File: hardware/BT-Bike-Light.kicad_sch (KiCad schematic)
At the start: 15 parts, among them J1 Conn_ARM_JTAG_SWD_10, J2 USB_C_Receptacle_USB2.0_16P, J3 Conn_01x02, Q1 Q_NMOS_GDS, SW1 SW_Push, U1 BC805M, U2 LIS2DTW12, U3 PAM2808, U4 BQ297xy, U5 MCP73834-xxx-MF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

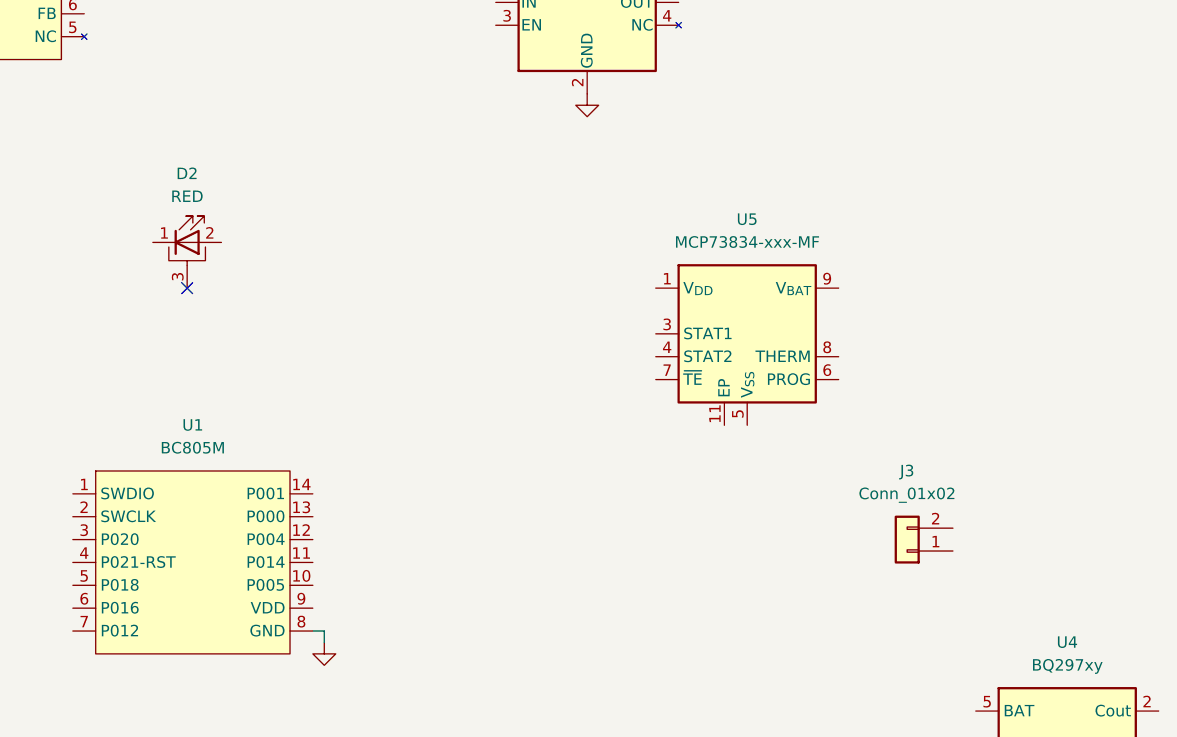
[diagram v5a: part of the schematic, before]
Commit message: Update battery connector
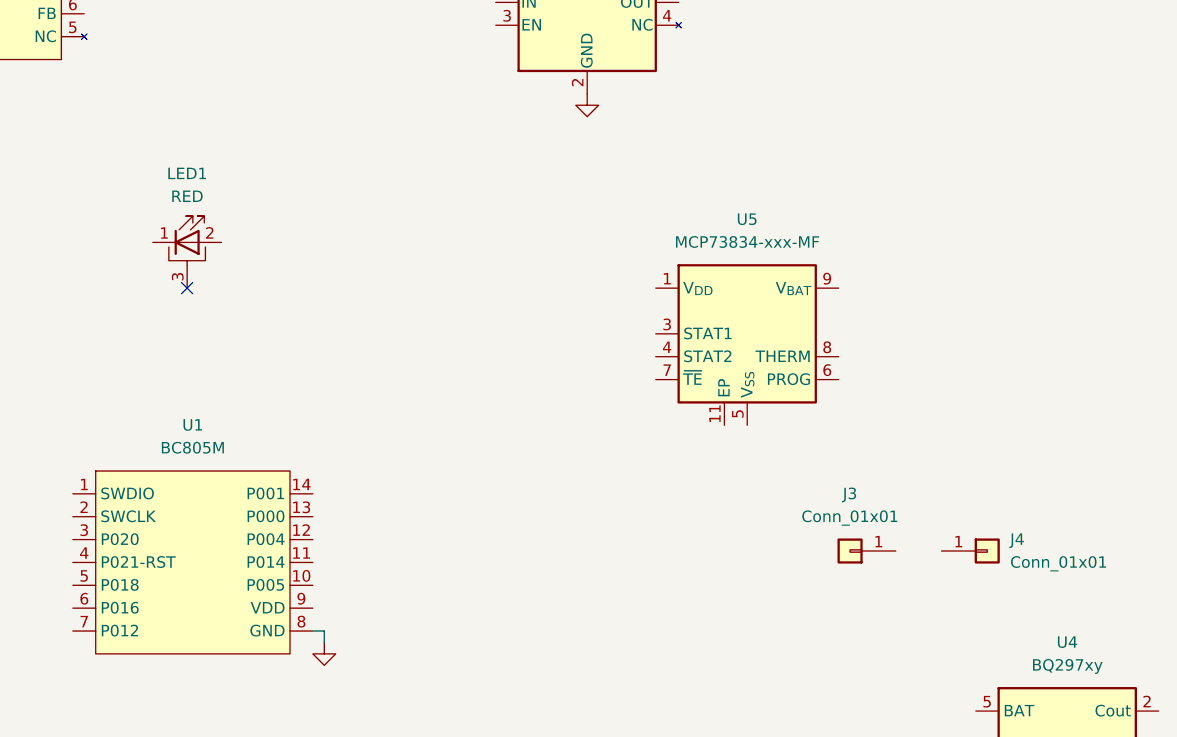
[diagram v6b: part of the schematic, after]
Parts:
- removed J3: Conn_01x02, symbol Connector_Generic:Conn_01x02
- added J3, J4: Conn_01x01, Battery:BatteryClip_Keystone_54_D16-19mm, symbol Connector_Generic:Conn_01x01
- renumbered D2 to LED1
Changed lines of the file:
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@@
+	)
+	(symbol
+		(lib_id "Connector_Generic:Conn_01x01")
+		(at 228.6 99.06 0)
+		(unit 1)
+		(exclude_from_sim no)
+		(in_bom yes)
+		(on_board yes)
+		(dnp no)
+		(fields_autoplaced yes)
+		(property "Reference" "J4"
+			(at 231.14 97.7899 0)
+			(effects
+				(font
+					(size 1.27 1.27)
+				)
+				(justify left)
+			)
+		)
+		(property "Value" "Conn_01x01"
+			(at 231.14 100.3299 0)
+			(effects
+				(font
+					(size 1.27 1.27)
+				)
+				(justify left)
+			)
+		)
+		(property "Footprint" "Battery:BatteryClip_Keystone_54_D16-19mm"
+			(at 228.6 99.06 0)
+			(effects
+				(font
+					(size 1.27 1.27)
+				)
+				(hide yes)
+			)
+		)
+		(property "Datasheet" "https://www.keyelco.com/userAssets/file/M65p11.pdf"
+			(at 228.6 99.06 0)
+			(effects
+				(font
+					(size 1.27 1.27)
+				)
+				(hide yes)
+			)
+		)
+		(property "Description" "Generic connector, single row, 01x01, script generated (kicad-library-utils/schlib/autogen/connector/)"
+			(at 228.6 99.06 0)
+			(effects
+				(font
+					(size 1.27 1.27)
+				)
+				(hide yes)
+			)
+		)
+		(pin "1"
+		)
+		(instances
+			(project ""
+				(path "/3263b444-391f-435a-aeab-6f7fca8830e2"
+					(reference "J4")
+					(unit 1)
+				)
+			)
+		)
+	)
+	(symbol
+		(lib_id "Connector_Generic:Conn_01x01")
+		(at 213.36 99.06 180)
+		(unit 1)
+		(exclude_from_sim no)
+		(in_bom yes)
+		(on_board yes)
+		(dnp no)
+		(fields_autoplaced yes)
+		(property "Reference" "J3"
+			(at 213.36 92.71 0)
+			(effects
+				(font
+					(size 1.27 1.27)
+				)
+			)
+		)
+		(property "Value" "Conn_01x01"
+			(at 213.36 95.25 0)
+			(effects
+				(font
+					(size 1.27 1.27)
+				)
+			)
+		)
+		(property "Footprint" "Battery:BatteryClip_Keystone_54_D16-19mm"
+			(at 213.36 99.06 0)
+			(effects
+				(font
+					(size 1.27 1.27)
+				)
+				(hide yes)
+			)
+		)
+		(property "Datasheet" "https://www.keyelco.com/userAssets/file/M65p11.pdf"
+			(at 213.36 99.06 0)
+			(effects
+				(font
+					(size 1.27 1.27)
+				)
+				(hide yes)
+			)
+		)
+		(property "Description" "Generic connector, single row, 01x01, script generated (kicad-library-utils/schlib/autogen/connector/)"
+			(at 213.36 99.06 0)
+			(effects
+				(font
+					(size 1.27 1.27)
+				)
+				(hide yes)
+			)
+		)
+		(pin "1"
+		)
+		(instances
+			(project "BT-Bike-Light"
+				(path "/3263b444-391f-435a-aeab-6f7fca8830e2"
+					(reference "J3")
+					(unit 1)
+				)
+			)
+		)
 	)
 	(symbol
@@
 		(dnp no)
 		(fields_autoplaced yes)
-		(property "Reference" "D2"
+		(property "Reference" "LED1"
 			(at 139.7 57.15 0)
 			(effects
@@
 			(project ""
 				(path "/3263b444-391f-435a-aeab-6f7fca8830e2"
-					(reference "D2")
+					(reference "LED1")
 					(unit 1)
 				)
@@
 					(unit 1)
 				)
-			)
-		)
-	)
-	(symbol
-		(lib_id "Connector_Generic:Conn_01x02")
-		(at 219.71 99.06 180)
-		(unit 1)
-		(exclude_from_sim no)
-		(in_bom yes)
-		(on_board yes)
-		(dnp no)
-		(fields_autoplaced yes)
-		(property "Reference" "J3"
-			(at 219.71 90.17 0)
-			(effects
-				(font
-					(size 1.27 1.27)
-				)
-			)
-		)
-		(property "Value" "Conn_01x02"
-			(at 219.71 92.71 0)
-			(effects
-				(font
-					(size 1.27 1.27)
-				)
-			)
-		)
-		(property "Footprint" ""
-			(at 219.71 99.06 0)
-			(effects
-				(font
-					(size 1.27 1.27)
-				)
-				(hide yes)
-			)
-		)
-		(property "Datasheet" "~"
-			(at 219.71 99.06 0)
-			(effects
-				(font
-					(size 1.27 1.27)
-				)
-				(hide yes)
-			)
-		)
-		(property "Description" "Generic connector, single row, 01x02, script generated (kicad-library-utils/schlib/autogen/connector/)"
-			(at 219.71 99.06 0)
-			(effects
-				(font
-					(size 1.27 1.27)
-				)
-				(hide yes)
-			)
-		)
-		(pin "2"
-		)
-		(pin "1"
-		)
-		(instances
-			(project ""
-				(path "/3263b444-391f-435a-aeab-6f7fca8830e2"
-					(reference "J3")
-					(unit 1)
-				)

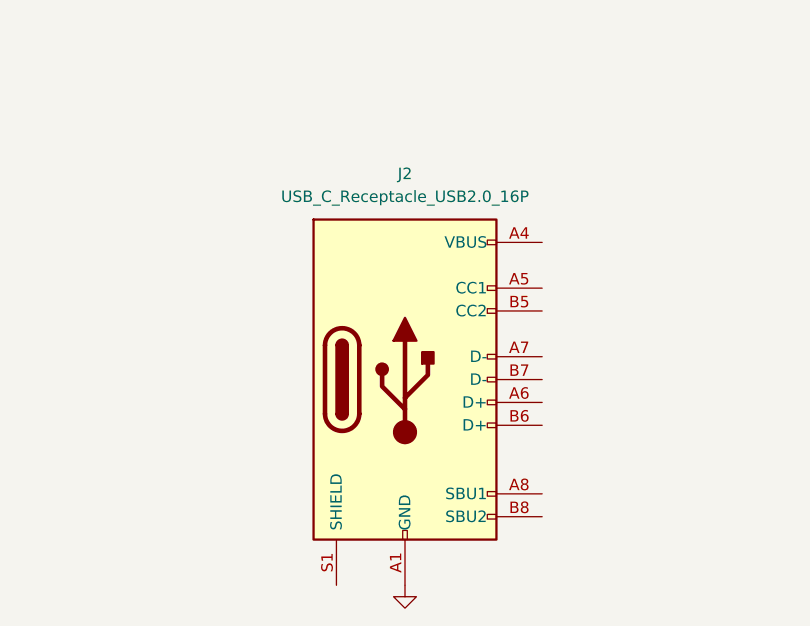
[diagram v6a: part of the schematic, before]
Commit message: Update USB-C receptacle
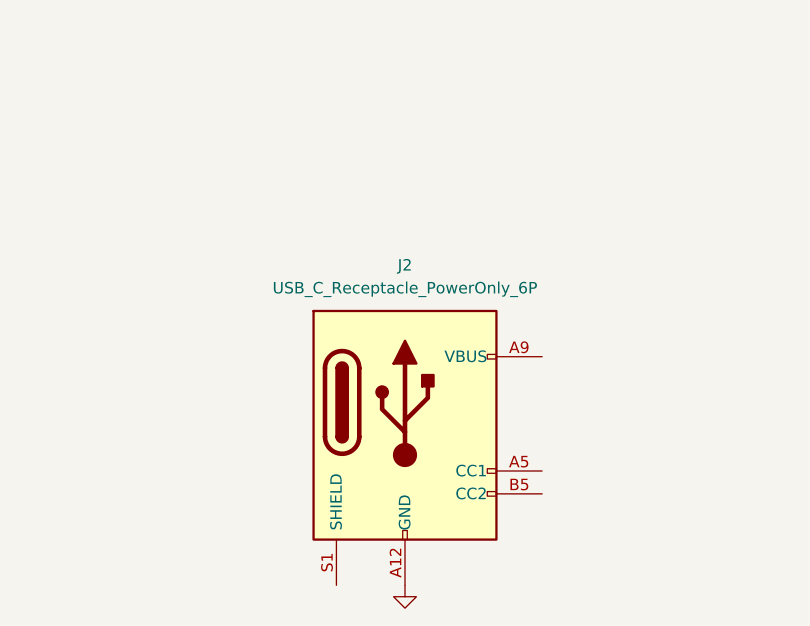
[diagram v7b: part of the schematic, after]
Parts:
- removed J2: USB_C_Receptacle_USB2.0_16P, GCT:USB_C_Receptacle_GCT_USB4145, symbol Connector:USB_C_Receptacle_USB2.0_16P
- added J2: USB_C_Receptacle_PowerOnly_6P, CUI-Devices:UJC-HP2-3-SMT-TR, symbol Connector:USB_C_Receptacle_PowerOnly_6P
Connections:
- net GND: now also J2.A12 (GND), J2.B12 (GND)
- new net: J2.A9 (VBUS), J2.B9 (VBUS)
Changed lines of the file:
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@@
-	)
-	(symbol
-		(lib_id "Connector:USB_C_Receptacle_USB2.0_16P")
-		(at 87.63 160.02 0)
-		(unit 1)
-		(exclude_from_sim no)
-		(in_bom yes)
-		(on_board yes)
-		(dnp no)
-		(fields_autoplaced yes)
-		(property "Reference" "J2"
-			(at 87.63 137.16 0)
-			(effects
-				(font
-					(size 1.27 1.27)
-				)
-			)
-		)
-		(property "Value" "USB_C_Receptacle_USB2.0_16P"
-			(at 87.63 139.7 0)
-			(effects
-				(font
-					(size 1.27 1.27)
-				)
-			)
-		)
-		(property "Footprint" "GCT:USB_C_Receptacle_GCT_USB4145"
-			(at 91.44 160.02 0)
-			(effects
-				(font
-					(size 1.27 1.27)
-				)
-				(hide yes)
-			)
-		)
-		(property "Datasheet" "https://www.usb.org/sites/default/files/documents/usb_type-c.zip"
-			(at 91.44 160.02 0)
-			(effects
-				(font
-					(size 1.27 1.27)
-				)
-				(hide yes)
-			)
-		)
-		(property "Description" "USB 2.0-only 16P Type-C Receptacle connector"
-			(at 87.63 160.02 0)
-			(effects
-				(font
-					(size 1.27 1.27)
-				)
-				(hide yes)
-			)
-		)
-		(pin "A12"
-		)
-		(pin "A6"
-		)
-		(pin "A8"
-		)
-		(pin "S1"
-		)
-		(pin "A4"
-		)
-		(pin "A7"
-		)
-		(pin "A5"
-		)
-		(pin "B8"
-		)
-		(pin "B7"
-		)
-		(pin "B9"
-		)
-		(pin "B1"
-		)
-		(pin "A1"
-		)
-		(pin "B6"
-		)
-		(pin "B5"
-		)
-		(pin "A9"
-		)
-		(pin "B4"
-		)
-		(pin "B12"
-		)
-		(instances
-			(project ""
-				(path "/3263b444-391f-435a-aeab-6f7fca8830e2"
-					(reference "J2")
-					(unit 1)
-				)
-			)
-		)
 	)
 	(symbol
@@
 					(unit 1)
 				)
+			)
+		)
+	)
+	(symbol
+		(lib_id "Connector:USB_C_Receptacle_PowerOnly_6P")
+		(at 87.63 165.1 0)
+		(unit 1)
+		(exclude_from_sim no)
+		(in_bom yes)
+		(on_board yes)
+		(dnp no)
+		(fields_autoplaced yes)
+		(property "Reference" "J2"
+			(at 87.63 147.32 0)
+			(effects
+				(font
+					(size 1.27 1.27)
+				)
+			)
+		)
+		(property "Value" "USB_C_Receptacle_PowerOnly_6P"
+			(at 87.63 149.86 0)
+			(effects
+				(font
+					(size 1.27 1.27)
+				)
+			)
+		)
+		(property "Footprint" "CUI-Devices:UJC-HP2-3-SMT-TR"
+			(at 91.44 162.56 0)
+			(effects
+				(font
+					(size 1.27 1.27)
+				)
+				(hide yes)
+			)
+		)
+		(property "Datasheet" "https://www.usb.org/sites/default/files/documents/usb_type-c.zip"
+			(at 87.63 165.1 0)
+			(effects
+				(font
+					(size 1.27 1.27)
+				)
+				(hide yes)
+			)
+		)
+		(property "Description" "USB Power-Only 6P Type-C Receptacle connector"
+			(at 87.63 165.1 0)
+			(effects
+				(font
+					(size 1.27 1.27)
+				)
+				(hide yes)
+			)
+		)
+		(pin "B5"
+		)
+		(pin "A5"
+		)
+		(pin "A12"
+		)
+		(pin "B12"
+		)
+		(pin "A9"
+		)
+		(pin "S1"
+		)
+		(pin "B9"
+		)
+		(instances
+			(project ""
+				(path "/3263b444-391f-435a-aeab-6f7fca8830e2"
+					(reference "J2")
+					(unit 1)
+				)

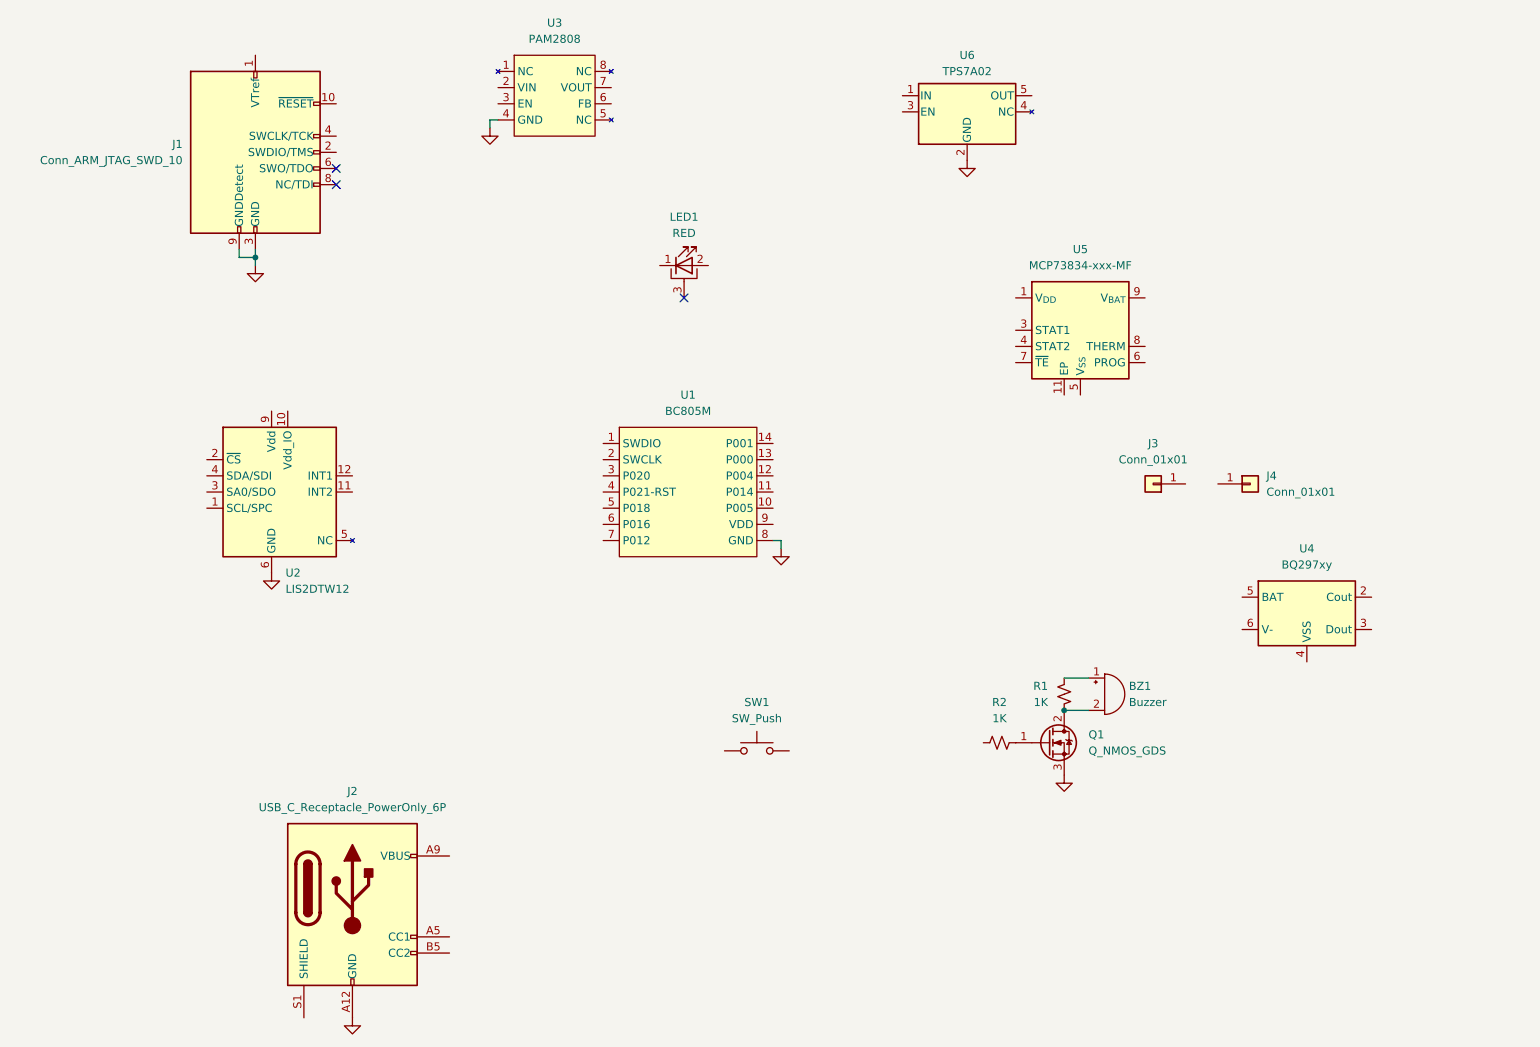
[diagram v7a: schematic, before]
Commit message: Add supporting electronics for LDO
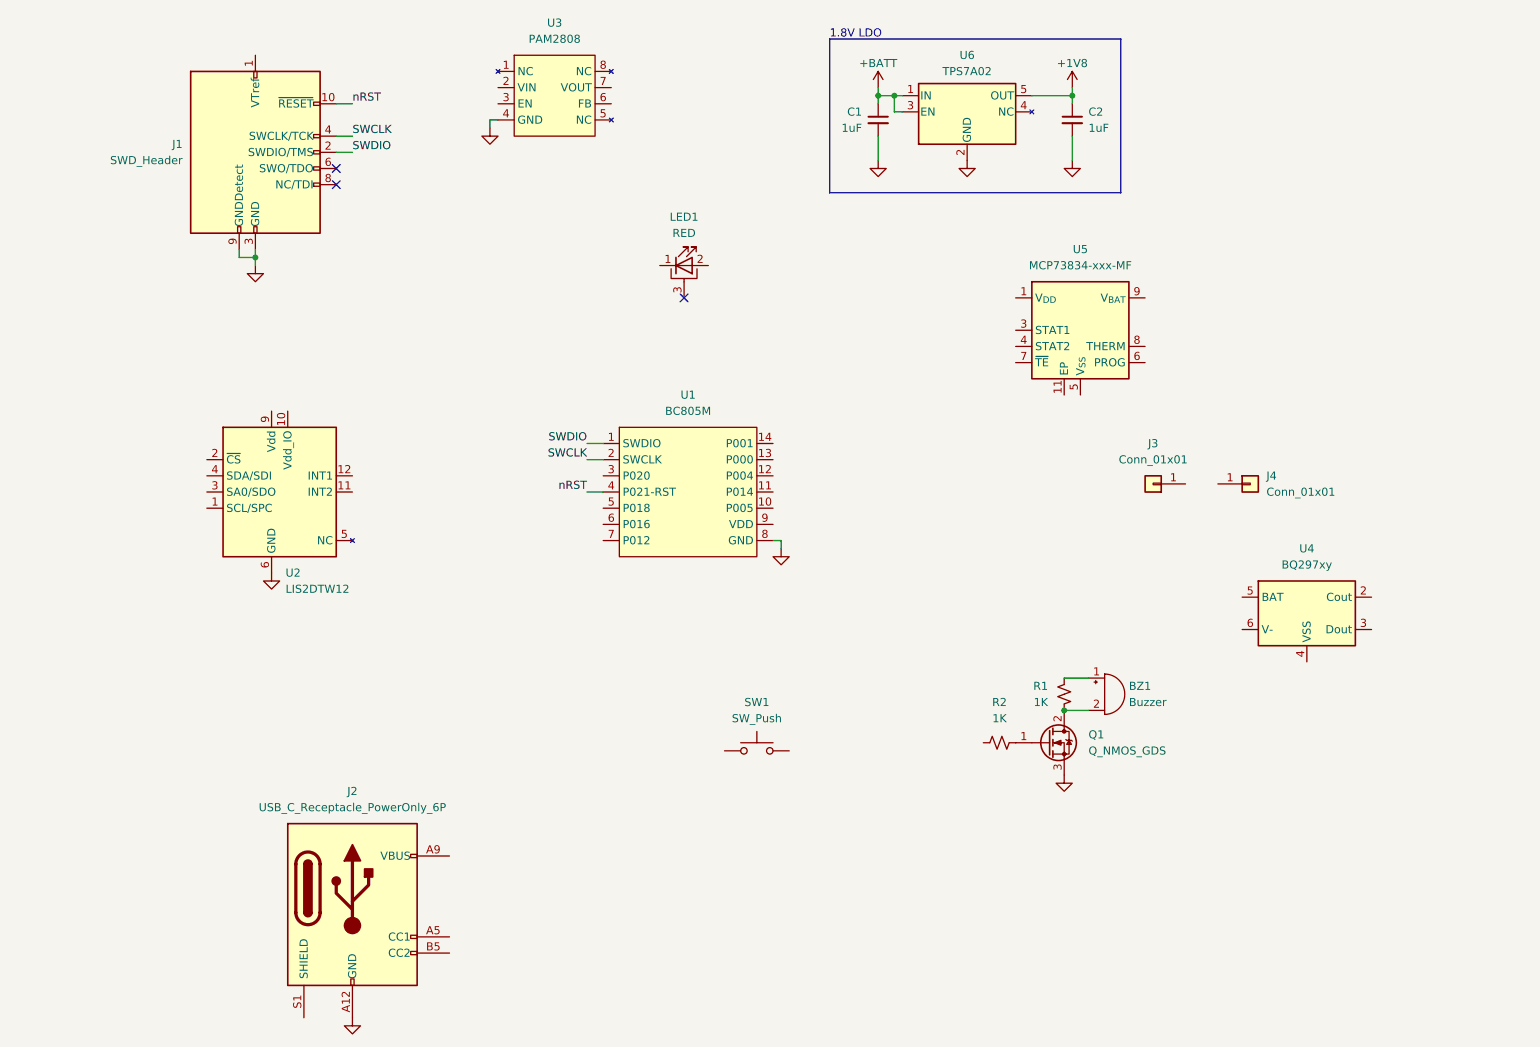
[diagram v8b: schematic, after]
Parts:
- added C1, C2: 1uF, symbol Device:C_Small
- J1: value Conn_ARM_JTAG_SWD_10 -> SWD_Header
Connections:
- net GND: now also C1.2, C2.2
- net SWDIO: now reaches U1.1 (SWDIO)
- net SWDIO: now also J1.2 (SWDIO/TMS)
- net SWCLK: now reaches U1.2 (SWCLK)
- net SWCLK: now also J1.4 (SWCLK/TCK)
- net nRST: now reaches U1.4 (P021-RST)
- net nRST: now also J1.10 (~{RESET})
- net +BATT: now reaches U6.1 (IN)
- net +BATT: now also U6.3 (EN), C1.1
- net +1V8: now reaches U6.5 (OUT)
- net +1V8: now also C2.1
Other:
- note added: "1.8V LDO"
